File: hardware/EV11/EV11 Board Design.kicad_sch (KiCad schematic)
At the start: 115 parts, among them CN1 PJ-313E-8A_C707222, CN2 X1270WVS-2X05B-6TV01, CN3 WAFER-SH1.0-6PWB, CN4 WAFER-SH1.0-6PWB, CN5 Debug_2, CN6 Debug_1, J1 Conn_01x02_Socket, J10 Conn_01x08_Socket, J2 Conn_01x01_Male, J3 Conn_01x01_Male, J9 USB_C_Receptacle, SW1 TS-1037-A11B3-D2, SW2 MSK12C02-HB, SW3 TS-1037-A11B3-D2, SW4 SW_Push, SW5 SW_Push, U1 STM32F405RGTx, U11 ESP32-S3-WROOM-1-N8R2, U13 BM14B(0.8)-24DS-0.4V(53), U2 BQ21040DBVR, U3 CH340C, U4 USBLC6-2P6, U5 M24C02-RMN6TP, U6 WM8960CGEFL/RV, U7 TPS63060, U8 STM32F072C8T6, Y1 Crystal_GND24

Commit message: EV11 is ready for production, hopefully
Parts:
- removed R28, R29: 0, Resistor_SMD:R_0402_1005Metric, symbol Device:R
- added CN7: Debug_3, X1270WVS-2x05B-6TV01:IDC-SMD_10P-P1.27_X1270WVS-2X05B-6TV01, symbol X1270WVS-2x05B-6TV01:X1270WVS-2X05B-6TV01
- added R28, R29, R36, R37, R38, R39, R40, R41: 1k0, Resistor_SMD:R_0402_1005Metric, symbol Device:R_US
- C1, C2: JLCPCB# (none) -> C15525
- C23, C4: value 33P -> 33p
- C37, C40, C42: JLCPCB# (none) -> C49678
- C38, C39, C43, C44, C45, C46, C47, C48: JLCPCB# (none) -> C15850
- C41: JLCPCB# (none) -> C1801
- D1: footprint Diode_SMD:D_0805_2012Metric -> Diode_SMD:D_0603_1608Metric; JLCPCB# (none) -> C2286
- D2, D6: JLCPCB# (none) -> C191023
- J2, J3: footprint Connector_PinHeader_1.00mm:PinHeader_1x01_P1.00mm_Vertical -> Connector_PinHeader_2.54mm:PinHeader_1x01_P2.54mm_Vertical
- L1: JLCBPCB# (none) -> C1042
- R1, R21: symbol Device:R -> Device:R_US; JLCPCB# (none) -> C25741
- R10, R11, R12, R13, R14, R15, R16, R17, R18, R2, R23, R24, R25, R3, R30, R31, R32, R33, R34, R35, R4, R5, R6, R7, R8, R9: symbol Device:R -> Device:R_US
- R19: symbol Device:R -> Device:R_US; JLCPCB# (none) -> C45956
- R20: symbol Device:R -> Device:R_US; JLCPCB# (none) -> C26984
- R22: symbol Device:R -> Device:R_US; JLCPCB# (none) -> C25744
- R26: footprint Resistor_SMD:R_0402_1005Metric -> Resistor_SMD:R_0603_1608Metric; symbol Device:R -> Device:R_US; JLCPCB# (none) -> C23228
- R27: symbol Device:R -> Device:R_US; JLCPCB# (none) -> C25867
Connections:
- net SPI1_MISO is gone; now on net MAIN_LED_R: U1.22 (PA6)
- net +3.3V: now also CN7.2
- net GND: now also CN7.4
- net MAIN_LED_B: now also U1.15 (PA1); no longer U1.4 (PC15)
- net MAIN_LED_G: now also U1.14 (PA0); no longer U1.8 (PC0)
- net MAIN_LED_R: no longer U1.9 (PC1)
- net PTT_AI_BTN: now also R29.2
- net PTT_BTN: now also R28.2
- net at D2.2 (A), SW2.2: now also R34.2
- net at C2.1, J1.2 (Pin_2), J2.1 (Pin_1)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: no longer R34.2
- net MAIN_DEBUG_1: now reaches U1.20 (PA4)
- net MAIN_DEBUG_1: now also R39.1
- net MAIN_DEBUG_3: now reaches U1.44 (PA11)
- net MAIN_DEBUG_3: now also R41.1
- net MAIN_DEBUG_2: now reaches U1.45 (PA12)
- net MAIN_DEBUG_2: now also R40.1
- net NET_DEBUG_1: now reaches U11.7 (IO7)
- net NET_DEBUG_1: now also R38.1
- net NET_DEBUG_2: now reaches U11.8 (IO15)
- net NET_DEBUG_2: now also R37.1
- net NET_DEBUG_3: now reaches U11.9 (IO16)
- net NET_DEBUG_3: now also R36.1
- net DISP_RSTR renamed DISP_RST
- new net: CN7.5, R36.2
- new net: CN7.1, R38.2
- new net: R28.1, U1.8 (PC0)
- new net: CN7.10, R41.2
- new net: CN7.3, R37.2
- new net: CN7.6, R39.2
- new net: CN7.8, R40.2
- new net: R29.1, U1.9 (PC1)
- no-connect marks 83 -> 79
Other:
- moved on the sheet: D2, D6

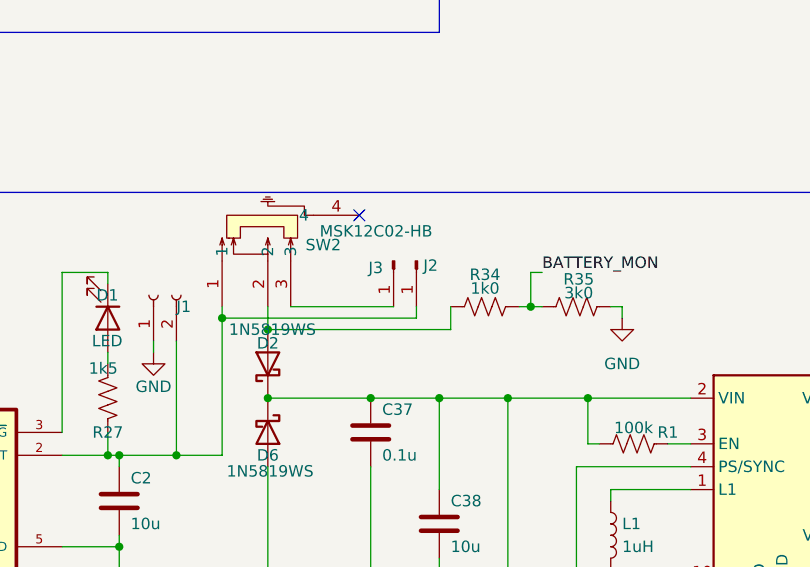
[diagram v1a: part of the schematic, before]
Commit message: Fixed jlcpcb fab attributes
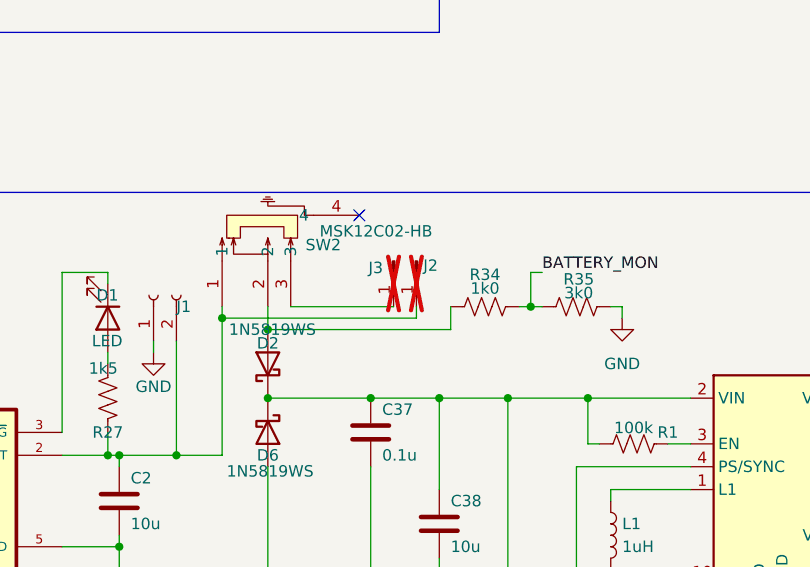
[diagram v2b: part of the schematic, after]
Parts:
- 120R1: JLCPCB Part # (none) -> C127301; JLCPCB# C127301 -> (none)
- C1, C2: JLCPCB Part # (none) -> C15525; JLCPCB# C15525 -> (none)
- C10, C18, C5, C9: JLCPCB Part # (none) -> C52923; JLCPCB# C52923 -> (none)
- C11, C12, C13, C14, C15, C16, C24, C25, C26, C32, C33, C34, C35, C36, C7: JLCPCB Part # (none) -> C1525; JLCPCB# C1525 -> (none)
- C21, C22: JLCPCB Part # (none) -> C12530; JLCPCB# C12530 -> (none)
- C23, C4: JLCPCB Part # (none) -> C107115; JLCPCB# C107115 -> (none)
- C28, C3, C31, C6: JLCPCB Part # (none) -> C23733; JLCPCB# C23733 -> (none)
- C29, C30: JLCPCB Part # (none) -> C15008; JLCPCB# C15008 -> (none)
- C37, C40, C42: JLCPCB Part # (none) -> C49678; JLCPCB# C49678 -> (none)
- C38, C39, C43, C44, C45, C46, C47, C48: JLCPCB Part # (none) -> C15850; JLCPCB# C15850 -> (none)
- C41: JLCPCB Part # (none) -> C1801; JLCPCB# C1801 -> (none)
- C8: JLCPCB Part # (none) -> C15195; JLCPCB# C15195 -> (none)
- CN1: JLCPCB Part # (none) -> C707222; JLCPCB Position Offset (none) -> 0,-0.5715; JLCPCB# C707222 -> (none); LCSC Part C707222 -> (none)
- CN2, CN5, CN6, CN7: JLCPCB Part # (none) -> C2962219; JLCPCB# C2962219 -> (none)
- CN3, CN4: JLCPCB Part # (none) -> C3029345; JLCPCB# C3029345 -> (none)
- D1: footprint Diode_SMD:D_0603_1608Metric -> Diode_SMD:D_0805_2012Metric; JLCPCB Part # (none) -> C130114; JLCPCB# C2286 -> (none)
- D2, D6: JLCPCB Part # (none) -> C191023; JLCPCB# C191023 -> (none)
- J1: JLCPCB Part # (none) -> C295747; JLCPCB Rotation Offset (none) -> 180
- J10: JLCPCB Part # (none) -> C3029347; JLCPCB Position Offset (none) -> 0,-0.1270
- J2, J3: now not fitted
- J9: JLCPCB Part # (none) -> C165948; JLCPCB Position Offset (none) -> 0,0.9525; JLCPCB# C165948 -> (none)
- L1: JLCBPCB# C1042 -> (none); JLCPCB Part # (none) -> C370013
- MAIN_LED1, MGMT_LEDA1, MGMT_LEDB1, NET_LED1: JLCPCB Part # (none) -> C2874115; JLCPCB# C2874115 -> (none)
- R1, R21: JLCPCB Part # (none) -> C25741; JLCPCB# C25741 -> (none)
- R10, R32, R5: JLCPCB Part # (none) -> C25900; JLCPCB# C25900 -> (none)
- R11, R12, R14, R15, R17, R18, R24, R25: JLCPCB Part # (none) -> C25082; JLCPCB# C25082 -> (none)
- R13, R16, R23, R6: JLCPCB Part # (none) -> C25087; JLCPCB# C25087 -> (none)
- R19: JLCPCB Part # (none) -> C45956; JLCPCB# C45956 -> (none)
- R2, R3: JLCPCB Part # (none) -> C25905; JLCPCB# C25905 -> (none)
- R20: JLCPCB Part # (none) -> C26984; JLCPCB# C26984 -> (none)
- R22: JLCPCB Part # (none) -> C25744; JLCPCB# C25744 -> (none)
- R26: footprint Resistor_SMD:R_0603_1608Metric -> Resistor_SMD:R_0402_1005Metric; JLCPCB Part # (none) -> C25130; JLCPCB# C23228 -> (none)
- R27, R7, R8: JLCPCB Part # (none) -> C25867; JLCPCB# C25867 -> (none)
- R28, R29, R31, R33, R34, R36, R37, R38, R39, R40, R41: JLCPCB Part # (none) -> C11702; JLCPCB# C11702 -> (none)
- R30: JLCPCB Part # (none) -> C17168; JLCPCB# C17168 -> (none)
- R35: JLCPCB Part # (none) -> C4211; JLCPCB# C4211 -> (none)
- R4: JLCPCB Part # (none) -> C25756; JLCPCB# C25756 -> (none)
- R9: JLCPCB Part # (none) -> C25879; JLCPCB# C25879 -> (none)
- SW1: JLCPCB Part # (none) -> C499331; JLCPCB Position Offset (none) -> 0,-0.625; JLCPCB# C499331 -> (none)
- SW2: JLCPCB Part # (none) -> C431541; JLCPCB Position Offset (none) -> 0, 0.635; LCSC Part C431541 -> (none)
- SW3: JLCPCB Part # (none) -> C499331; JLCPCB Position Offset (none) -> 0,-0.635; JLCPCB# C499331 -> (none)
- SW4, SW5: JLCPCB Part # (none) -> C266189; JLCPCB# C266189 -> (none)
- U1: JLCPCB Part # (none) -> C15742; JLCPCB# C15742 -> (none)
- U11: JLCPCB Part # (none) -> C3013944; JLCPCB Position Offset (none) -> 0,-0.254; JLCPCB# C3013944 -> (none)
- U13: JLCPCB Part # (none) -> C9900001863; JLCPCB Position Offset (none) -> 2.2225,0.889; JLCPCB# C9900001863 -> (none)
- U3: JLCPCB Part # (none) -> C84681; JLCPCB# C84681 -> (none)
- U4: JLCPCB Part # (none) -> C2827693; JLCPCB Rotation Offset (none) -> 270; JLCPCB# C2827693 -> (none)
- U5: JLCPCB Part # (none) -> C83836; JLCPCB Rotation Offset (none) -> 90; JLCPCB# C83836 -> (none)
- U6: JLCPCB Part # (none) -> C18752; JLCPCB# C18752 -> (none)
- U7: JLCPCB Rotation Offset (none) -> 270
- U8: JLCPCB Part # (none) -> C80488; JLCPCB# C80488 -> (none)
- Y1: JLCPCB Part # (none) -> C13738; JLCPCB# C13738 -> (none)

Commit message: Used previously used inductors, and caps for the switching power supply
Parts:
- C1, C2: JLCPCB Part # C15525 -> C307415
- C37, C40, C42: JLCPCB Part # C49678 -> C495959
- C38, C39, C43, C44, C45, C46, C47, C48: JLCPCB Part # C15850 -> C83061
- C41: JLCPCB Part # C1801 -> C519933
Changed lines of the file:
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@@
 			)
 		)
-		(property "JLCPCB Part #" "C49678"
+		(property "JLCPCB Part #" "C495959"
 			(at 203.2 320.04 0)
 			(effects
@@
 			)
 		)
-		(property "JLCPCB Part #" "C49678"
+		(property "JLCPCB Part #" "C495959"
 			(at 110.49 321.31 0)
 			(effects
@@
 			)
 		)
-		(property "JLCPCB Part #" "C15850"
+		(property "JLCPCB Part #" "C83061"
 			(at 218.44 332.74 0)
 			(effects
@@
 			)
 		)
-		(property "JLCPCB Part #" "C15850"
+		(property "JLCPCB Part #" "C83061"
 			(at 233.68 332.74 0)
 			(effects
@@
 			)
 		)
-		(property "JLCPCB Part #" "C15850"
+		(property "JLCPCB Part #" "C83061"
 			(at 241.3 326.39 0)
 			(effects
@@
 			)
 		)
-		(property "JLCPCB Part #" "C15525"
+		(property "JLCPCB Part #" "C307415"
 			(at 82.55 328.93 0)
 			(effects
@@
 			)
 		)
-		(property "JLCPCB Part #" "C15850"
+		(property "JLCPCB Part #" "C83061"
 			(at 118.11 331.47 0)
 			(effects
@@
 			)
 		)
-		(property "JLCPCB Part #" "C49678"
+		(property "JLCPCB Part #" "C495959"
 			(at 172.72 339.09 0)
 			(effects
@@
 			)
 		)
-		(property "JLCPCB Part #" "C15850"
+		(property "JLCPCB Part #" "C83061"
 			(at 226.06 339.09 0)
 			(effects
@@
 			)
 		)
-		(property "JLCPCB Part #" "C15525"
+		(property "JLCPCB Part #" "C307415"
 			(at 36.83 330.2 0)
 			(effects
@@
 			)
 		)
-		(property "JLCPCB Part #" "C15850"
+		(property "JLCPCB Part #" "C83061"
 			(at 125.73 340.36 0)
 			(effects
@@
 			)
 		)
-		(property "JLCPCB Part #" "C1801"
+		(property "JLCPCB Part #" "C519933"
 			(at 180.34 339.09 0)
 			(effects
@@
 			)
 		)
-		(property "JLCPCB Part #" "C15850"
+		(property "JLCPCB Part #" "C83061"
 			(at 210.82 326.39 0)
 			(effects
@@
 			)
 		)
-		(property "JLCPCB Part #" "C15850"
+		(property "JLCPCB Part #" "C83061"
 			(at 248.92 320.04 0)
 			(effects

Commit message: Bunch of cleanup
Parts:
- added JP1: SolderJumper_2_Bridged, Jumper:SolderJumper-2_P1.3mm_Bridged_RoundedPad1.0x1.5mm, symbol Jumper:SolderJumper_2_Bridged
- C29, C30: value 100U -> 100u
- C3, C6: value 4.7u -> 4u7
- C37, C40, C42: value 0.1u -> 100n
- C41: value 2.2p -> 2p2
- CN5: value Debug_2 -> Conn_05x02_Male
- CN6: value Debug_1 -> Conn_05x02_Male
- CN7: value Debug_3 -> Conn_05x02_Male
- L1: footprint Inductor_SMD:L_0805_2012Metric -> MCL2016A1R0MT:L0806
- L2: renamed from 120R1; value FerriteBead -> 120R1
- R20: value 64.9k -> 64k9
- SW1: JLCPCB Position Offset 0,-0.625 -> 0,-0.635
- U2: JLCPCB Part # (none) -> C202311
- U7: JLCPCB Part # (none) -> C48567
- renumbered MGMT_LEDA1 to D3, MGMT_LEDB1 to D4, NET_LED1 to D5, MAIN_LED1 to D7
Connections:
- net +3.3V: now also U7.10 (L2); no longer U7.9 (VOUT)
- net GND: now also U7.3 (EN), JP1.2 (B); no longer C5.1, CN1.4, U7.4 (PS/SYNC)
- net HP_L: now also CN1.4; no longer CN1.2
- net HP_R: now also CN1.5; no longer CN1.3
- net MIC_P: now also CN1.2; no longer CN1.5
- net at C41.1, R19.1, R20.2: no longer U7.8 (FB)
- net at C37.1, C38.1, C39.1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: now also U7.1 (L1); no longer U7.2 (VIN)
- net at L1.1: now also U7.6 (VAUX); no longer U7.1 (L1)
- net at L1.2: no longer U7.10 (L2)
- net at C40.1: no longer U7.6 (VAUX)
- net at R1.2: now also U7.2 (VIN); no longer U7.3 (EN)
- new net MIC_N: C5.1, CN1.3, JP1.1 (A)

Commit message: Cleaned up errors and warnings
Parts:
- removed C21, C22: 2u2, Capacitor_SMD:C_0402_1005Metric, symbol Device:C
- removed C33: 100n, Capacitor_SMD:C_0402_1005Metric, symbol Device:C
- added C17, C19: 2u2, Capacitor_SMD:C_0402_1005Metric, symbol Device:C
- added C20: 100n, Capacitor_SMD:C_0402_1005Metric, symbol Device:C
- J1: symbol Connector:Conn_01x02_Female -> Connector:Conn_01x02_Socket
- J10: symbol Connector:Conn_01x08_Female -> Connector:Conn_01x08_Socket
- J2: symbol Connector:Conn_01x01_Male -> Connector:Conn_01x01_Socket
- J3: value Conn_01x01_Male -> Conn_01x01_Socket; symbol Connector:Conn_01x01_Male -> Connector:Conn_01x01_Socket
- J9: symbol Connector:USB_C_Receptacle -> Connector:USB_C_Receptacle_USB2.0_16P; JLCPCB Position Offset 0,0.9525 -> 0,1.397
- JP1: footprint Jumper:SolderJumper-2_P1.3mm_Bridged_RoundedPad1.0x1.5mm -> NetTie:NetTie-2_SMD_Pad0.5mm; now left out of the parts list
- U11: footprint XCVR_ESP32-S3-WROOM-1-N8R2 -> RF_Module:ESP32-S3-WROOM-1U
- U5: footprint M24C02-RMN6TP:SOIC-8_L4.9-W3.9-P1.27-LS6.0-BL -> Package_SO:SOIC-8_3.9x4.9mm_P1.27mm; symbol M24C02-RMN6TP:M24C02-RMN6TP -> Memory_EEPROM:M24C02-RMN; JLCPCB Rotation Offset 90 -> (none)
- U6: footprint ESP32-S3-WROOM-1-N8R2:QFN50P500X500X90-33N -> Package_DFN_QFN:QFN-32-1EP_5x5mm_P0.5mm_EP3.3x3.3mm_ThermalVias
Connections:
- net +3.3V: now also U7.9 (VOUT), C20.2; no longer U7.10 (L2)
- net GND: now also R2.2, R3.2, U6.33 (EP), U7.4 (PS/SYNC), C17.1, C19.1, C20.1; no longer R2.1, R3.1, U7.3 (EN)
- net at C41.1, R19.1, R20.2: now also U7.8 (FB)
- net at C37.1, C38.1, C39.1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: now also U7.2 (VIN); no longer U7.1 (L1)
- net at L1.1: now also U7.1 (L1); no longer U7.6 (VAUX)
- net at L1.2: now also U7.10 (L2)
- net at J9.A5 (CC1), R33.2: now also R3.1; no longer R3.2
- net at J9.B5 (CC2), R31.2: now also R2.1; no longer R2.2
- net at U1.47 (VCAP_2): now also C19.2
- net at U1.31 (VCAP_1): now also C17.2
- net at C40.1: now also U7.6 (VAUX)
- net at R1.2: now also U7.3 (EN); no longer U7.2 (VIN)
- net MAIN_BOOT renamed UI_BOOT
- net MAIN_DEBUG_1 renamed UI_DEBUG_1
- net MAIN_DEBUG_2 renamed UI_DEBUG_2
- net MAIN_DEBUG_3 renamed UI_DEBUG_3
- net MAIN_LED_B renamed UI_LED_B
- net MAIN_LED_G renamed UI_LED_G
- net MAIN_LED_R renamed UI_LED_R
- net MAIN_NRST renamed UI_NRST
- net MAIN_RX1_MGMT renamed UI_RX1_MGMT
- net MAIN_RX2_NET renamed UI_RX2_NET
- net MAIN_SCL renamed UI_SCL
- net MAIN_SDA renamed UI_SDA
- net MAIN_STAT renamed UI_STAT
- net MAIN_SWCLK renamed UI_SWCLK
- net MAIN_SWDIO renamed UI_SWDIO
- net MAIN_TX1_MGMT renamed UI_TX1_MGMT
- net MAIN_TX2_NET renamed UI_TX2_NET
- no-connect marks 79 -> 70
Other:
- moved on the sheet: R2, R3, R31, R33

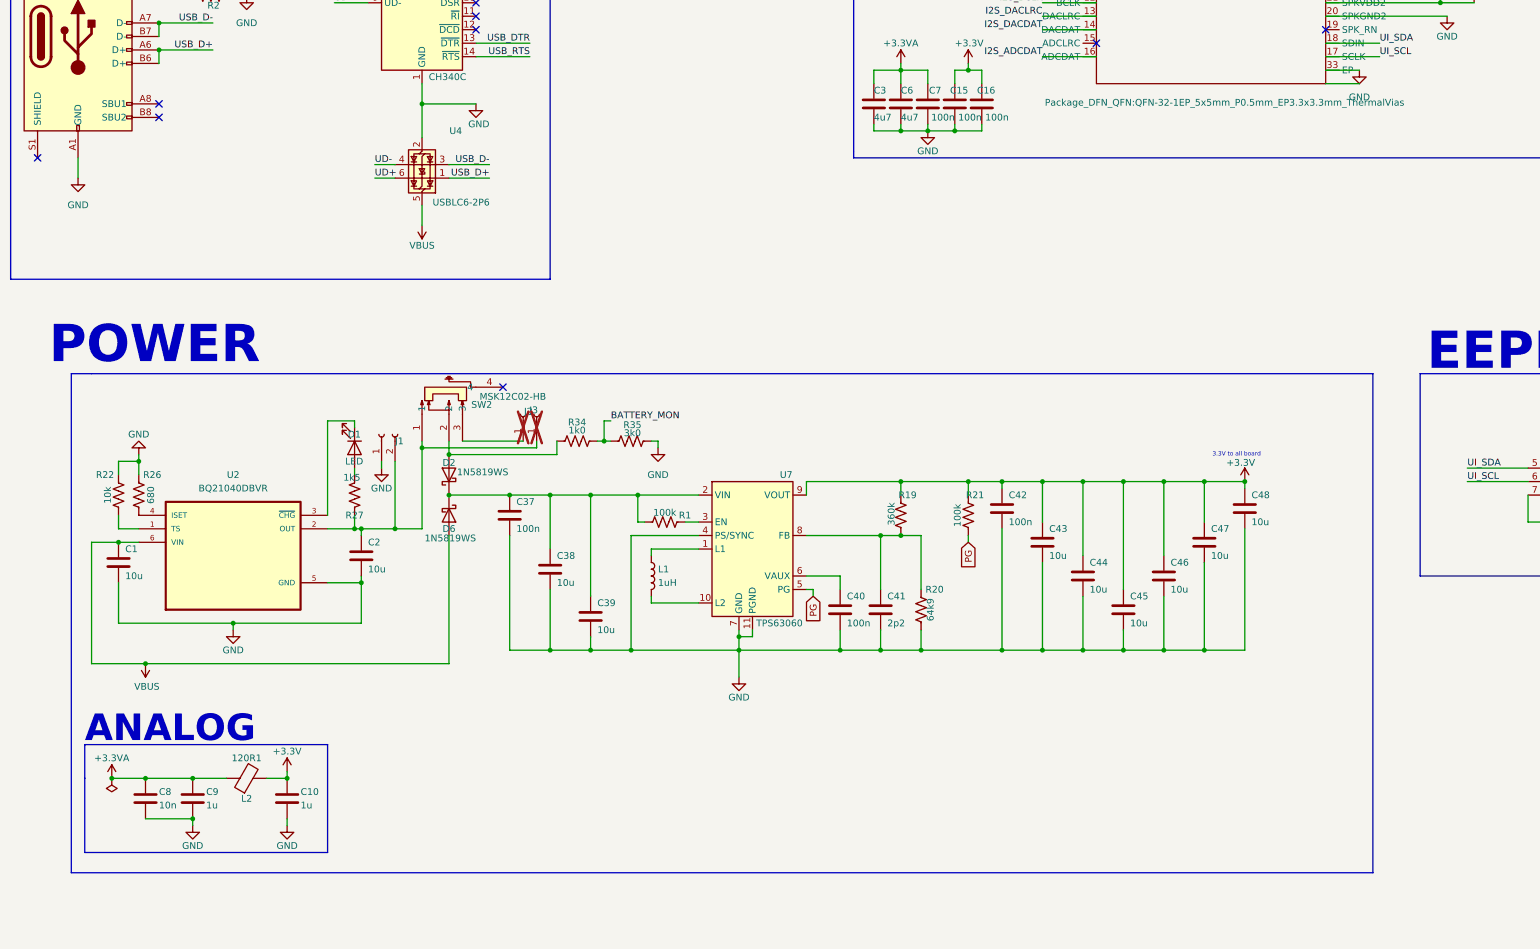
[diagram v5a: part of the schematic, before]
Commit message: Redesigned power schematic
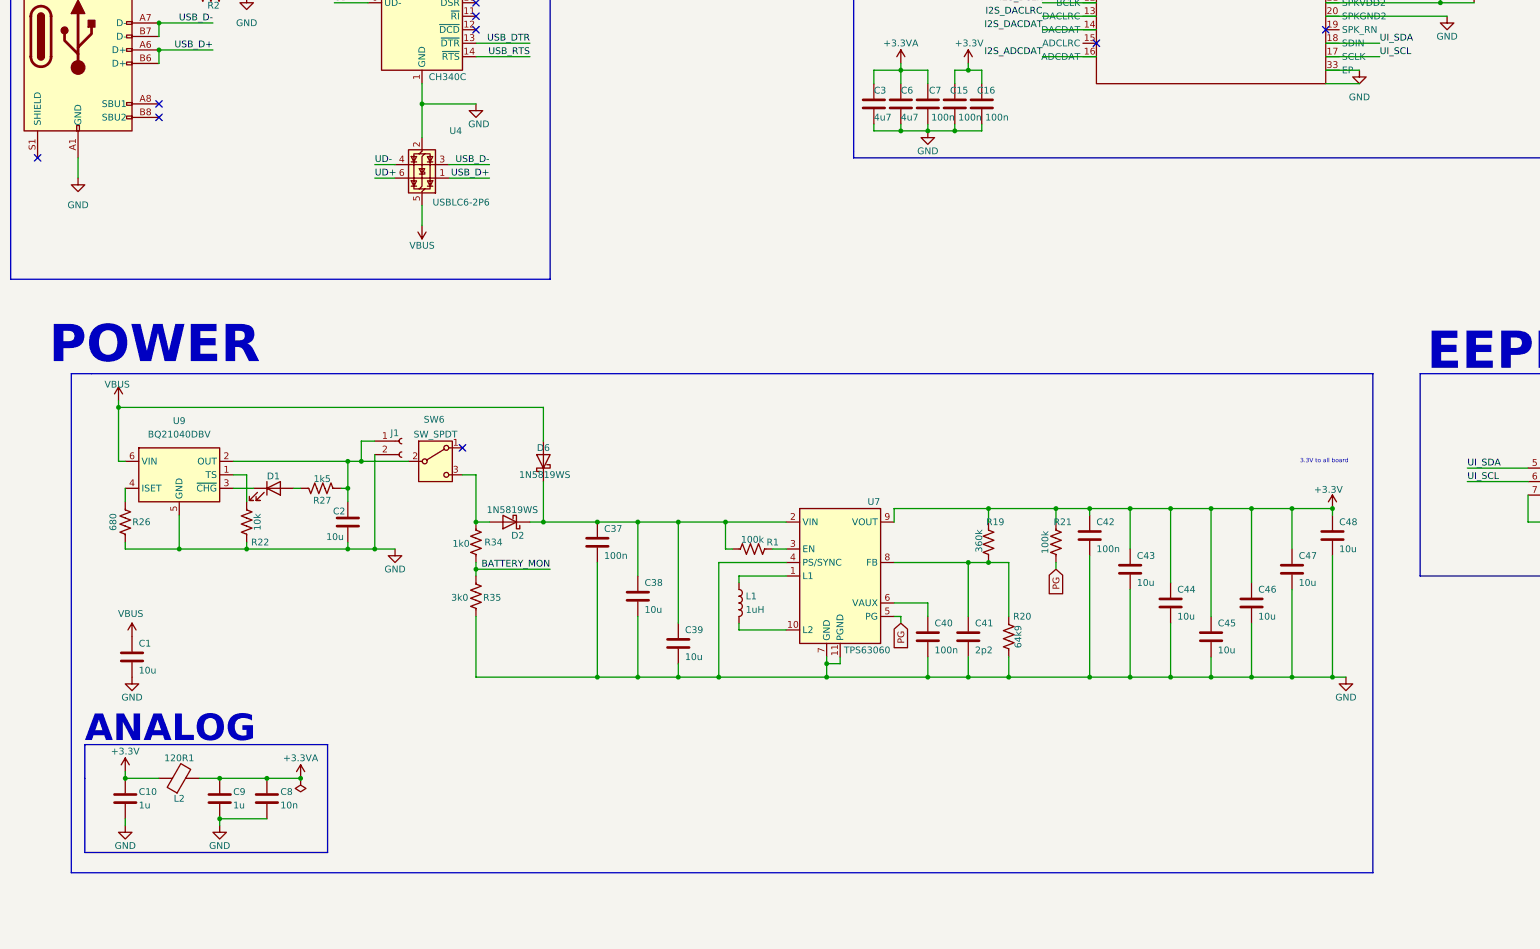
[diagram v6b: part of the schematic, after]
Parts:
- removed J2: Conn_01x01_Male, Connector_PinHeader_2.54mm:PinHeader_1x01_P2.54mm_Vertical, symbol Connector:Conn_01x01_Socket
- removed J3: Conn_01x01_Socket, Connector_PinHeader_2.54mm:PinHeader_1x01_P2.54mm_Vertical, symbol Connector:Conn_01x01_Socket
- removed SW2: MSK12C02-HB, :SW-TH_MSK12C02-HB-1, symbol MSK12C02-HB:MSK12C02-HB
- removed U2: BQ21040DBVR, BQ21040DBVR:SOT95P280X145-6N, symbol BQ21040DBVR:BQ21040DBVR
- added SW6: SW_SPDT, symbol Switch:SW_SPDT
- added U9: BQ21040DBV, Package_TO_SOT_SMD:SOT-23-6, symbol Battery_Management:BQ21040DBV
- CN1: LCSC Part (none) -> C707222
- CN2, CN5, CN6, CN7: JLCPCB# (none) -> C2962219
- CN3, CN4: JLCPCB# (none) -> C3029345
- D3, D4, D5, D7: JLCPCB# (none) -> C2874115
- SW1, SW3: LCSC Part (none) -> C499331
- U8: JLCPCB# (none) -> C80488
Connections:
- net +3.3V: now also L2.1; no longer L2.2
- net +3.3VA: now also L2.2; no longer L2.1
- net GND: now also J1.2 (Pin_2), U9.5 (GND); no longer J1.1 (Pin_1)
- net VBUS: now also U9.6 (VIN)
- net at R22.1: now also U9.1 (TS)
- net at D2.2 (A), R34.2: now also SW6.3 (C)
- net at R26.1: now also U9.4 (ISET)
- net at D1.1 (K): now also U9.3 (~{CHG})
- net at C2.1, R27.1: now also J1.1 (Pin_1), SW6.2 (B), U9.2 (OUT); no longer J1.2 (Pin_2)
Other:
- moved on the sheet: C1, C10, C2, C37, C38, C39, C40, C41, C42, C43, C44, C45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
